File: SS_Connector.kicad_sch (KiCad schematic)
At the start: 6 parts

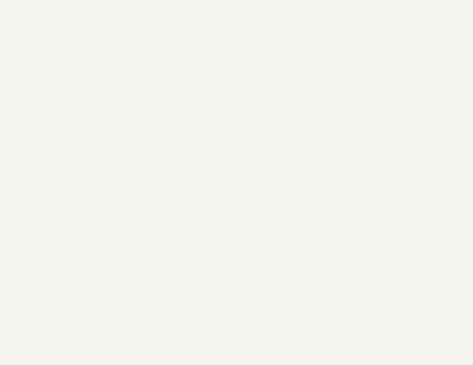
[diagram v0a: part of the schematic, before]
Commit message: MCU interfaces are done! Check the Changes and Complete ERC modifications
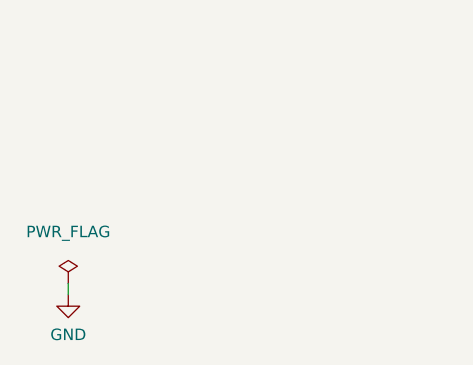
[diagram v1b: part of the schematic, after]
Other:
- company: (none) -> Parikshit Student Satellite Team
- title: (none) -> AOCS BOARD
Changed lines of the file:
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@@
 (kicad_sch (version 20211123) (generator eeschema)
   (paper "A4")
+  (title_block
+    (title "AOCS BOARD")
+    (company "Parikshit Student Satellite Team")
+  )
   (junction (at 199.39 45.72) (diameter 0) (color 0 0 0 0)
   )
@@
   )
   (wire (pts (xy 41.91 119.38) (xy 46.99 119.38))
+    (stroke (width 0) (type default) (color 0 0 0 0))
+  )
+  (wire (pts (xy 18.415 179.07) (xy 18.415 177.8))
     (stroke (width 0) (type default) (color 0 0 0 0))
   )
@@
   (symbol (lib_id "power:GND") (at 144.78 135.89 0) (unit 1)
     (in_bom yes) (on_board yes) (fields_autoplaced)
-    (property "Reference" "#PWR?" (id 0) (at 144.78 142.24 0)
+    (property "Reference" "#PWR0259" (id 0) (at 144.78 142.24 0)
       (effects (font (size 1.27 1.27)) hide)
     )
@@
   (symbol (lib_id "power:GND") (at 114.3 119.38 0) (unit 1)
     (in_bom yes) (on_board yes) (fields_autoplaced)
-    (property "Reference" "#PWR?" (id 0) (at 114.3 125.73 0)
+    (property "Reference" "#PWR0260" (id 0) (at 114.3 125.73 0)
       (effects (font (size 1.27 1.27)) hide)
     )
@@
   (symbol (lib_id "power:GND") (at 110.49 46.99 0) (unit 1)
     (in_bom yes) (on_board yes) (fields_autoplaced)
-    (property "Reference" "#PWR?" (id 0) (at 110.49 53.34 0)
+    (property "Reference" "#PWR0258" (id 0) (at 110.49 53.34 0)
       (effects (font (size 1.27 1.27)) hide)
     )
@@
   (symbol (lib_id "power:GND") (at 204.47 119.38 0) (unit 1)
     (in_bom yes) (on_board yes) (fields_autoplaced)
-    (property "Reference" "#PWR?" (id 0) (at 204.47 125.73 0)
+    (property "Reference" "#PWR0264" (id 0) (at 204.47 125.73 0)
       (effects (font (size 1.27 1.27)) hide)
     )
@@
     (pin "1")
   )
+  (symbol (lib_id "power:PWR_FLAG") (at 18.415 177.8 0) (unit 1)
+    (in_bom yes) (on_board yes) (fields_autoplaced)
+    (property "Reference" "#FLG0116" (id 0) (at 18.415 175.895 0)
+      (effects (font (size 1.27 1.27)) hide)
+    )
+    (property "Value" "PWR_FLAG" (id 1) (at 18.415 172.085 0))
+    (property "Footprint" "" (id 2) (at 18.415 177.8 0)
+      (effects (font (size 1.27 1.27)) hide)
+    )
+    (property "Datasheet" "~" (id 3) (at 18.415 177.8 0)
+      (effects (font (size 1.27 1.27)) hide)
+    )
+    (pin "1")
+  )
   (symbol (lib_id "power:GND") (at 73.66 135.89 0) (unit 1)
     (in_bom yes) (on_board yes) (fields_autoplaced)
-    (property "Reference" "#PWR?" (id 0) (at 73.66 142.24 0)
+    (property "Reference" "#PWR0253" (id 0) (at 73.66 142.24 0)
       (effects (font (size 1.27 1.27)) hide)
     )
@@
   (symbol (lib_id "power:GND") (at 199.39 48.26 0) (unit 1)
     (in_bom yes) (on_board yes) (fields_autoplaced)
-    (property "Reference" "#PWR?" (id 0) (at 199.39 54.61 0)
+    (property "Reference" "#PWR0255" (id 0) (at 199.39 54.61 0)
       (effects (font (size 1.27 1.27)) hide)
     )
@@
   (symbol (lib_id "power:GND") (at 41.91 121.92 0) (unit 1)
     (in_bom yes) (on_board yes) (fields_autoplaced)
-    (property "Reference" "#PWR?" (id 0) (at 41.91 128.27 0)
+    (property "Reference" "#PWR0254" (id 0) (at 41.91 128.27 0)
       (effects (font (size 1.27 1.27)) hide)
     )
@@
   (symbol (lib_id "power:GND") (at 142.24 63.5 0) (unit 1)
     (in_bom yes) (on_board yes) (fields_autoplaced)
-    (property "Reference" "#PWR?" (id 0) (at 142.24 69.85 0)
+    (property "Reference" "#PWR0257" (id 0) (at 142.24 69.85 0)
       (effects (font (size 1.27 1.27)) hide)
     )
@@
   (symbol (lib_id "power:GND") (at 232.41 133.35 0) (unit 1)
     (in_bom yes) (on_board yes) (fields_autoplaced)
-    (property "Reference" "#PWR?" (id 0) (at 232.41 139.7 0)
+    (property "Reference" "#PWR0263" (id 0) (at 232.41 139.7 0)
       (effects (font (size 1.27 1.27)) hide)
     )
@@
   (symbol (lib_id "power:GND") (at 50.8 48.26 0) (unit 1)
     (in_bom yes) (on_board yes) (fields_autoplaced)
-    (property "Reference" "#PWR?" (id 0) (at 50.8 54.61 0)
+    (property "Reference" "#PWR0261" (id 0) (at 50.8 54.61 0)
       (effects (font (size 1.27 1.27)) hide)
     )
@@
     (pin "MP2")
   )
+  (symbol (lib_id "power:GND") (at 18.415 179.07 0) (unit 1)
+    (in_bom yes) (on_board yes) (fields_autoplaced)
+    (property "Reference" "#PWR0280" (id 0) (at 18.415 185.42 0)
+      (effects (font (size 1.27 1.27)) hide)
+    )
+    (property "Value" "GND" (id 1) (at 18.415 183.515 0))
+    (property "Footprint" "" (id 2) (at 18.415 179.07 0)
+      (effects (font (size 1.27 1.27)) hide)
+    )
+    (property "Datasheet" "" (id 3) (at 18.415 179.07 0)
+      (effects (font (size 1.27 1.27)) hide)
+    )
+    (pin "1")
+  )
   (symbol (lib_id "power:GND") (at 229.87 63.5 0) (unit 1)
     (in_bom yes) (on_board yes) (fields_autoplaced)
-    (property "Reference" "#PWR?" (id 0) (at 229.87 69.85 0)
+    (property "Reference" "#PWR0256" (id 0) (at 229.87 69.85 0)
       (effects (font (size 1.27 1.27)) hide)
     )
@@
   (symbol (lib_id "power:GND") (at 78.74 63.5 0) (unit 1)
     (in_bom yes) (on_board yes) (fields_autoplaced)
-    (property "Reference" "#PWR?" (id 0) (at 78.74 69.85 0)
-      (effects (font (size 1.27 1.27)) hide)
-    )
+    (property "Reference" "#PWR0262" (id 0) (at 78.74 69.85 0)
+      (effects (font (size 1.27 1.27)) hide)
+    )

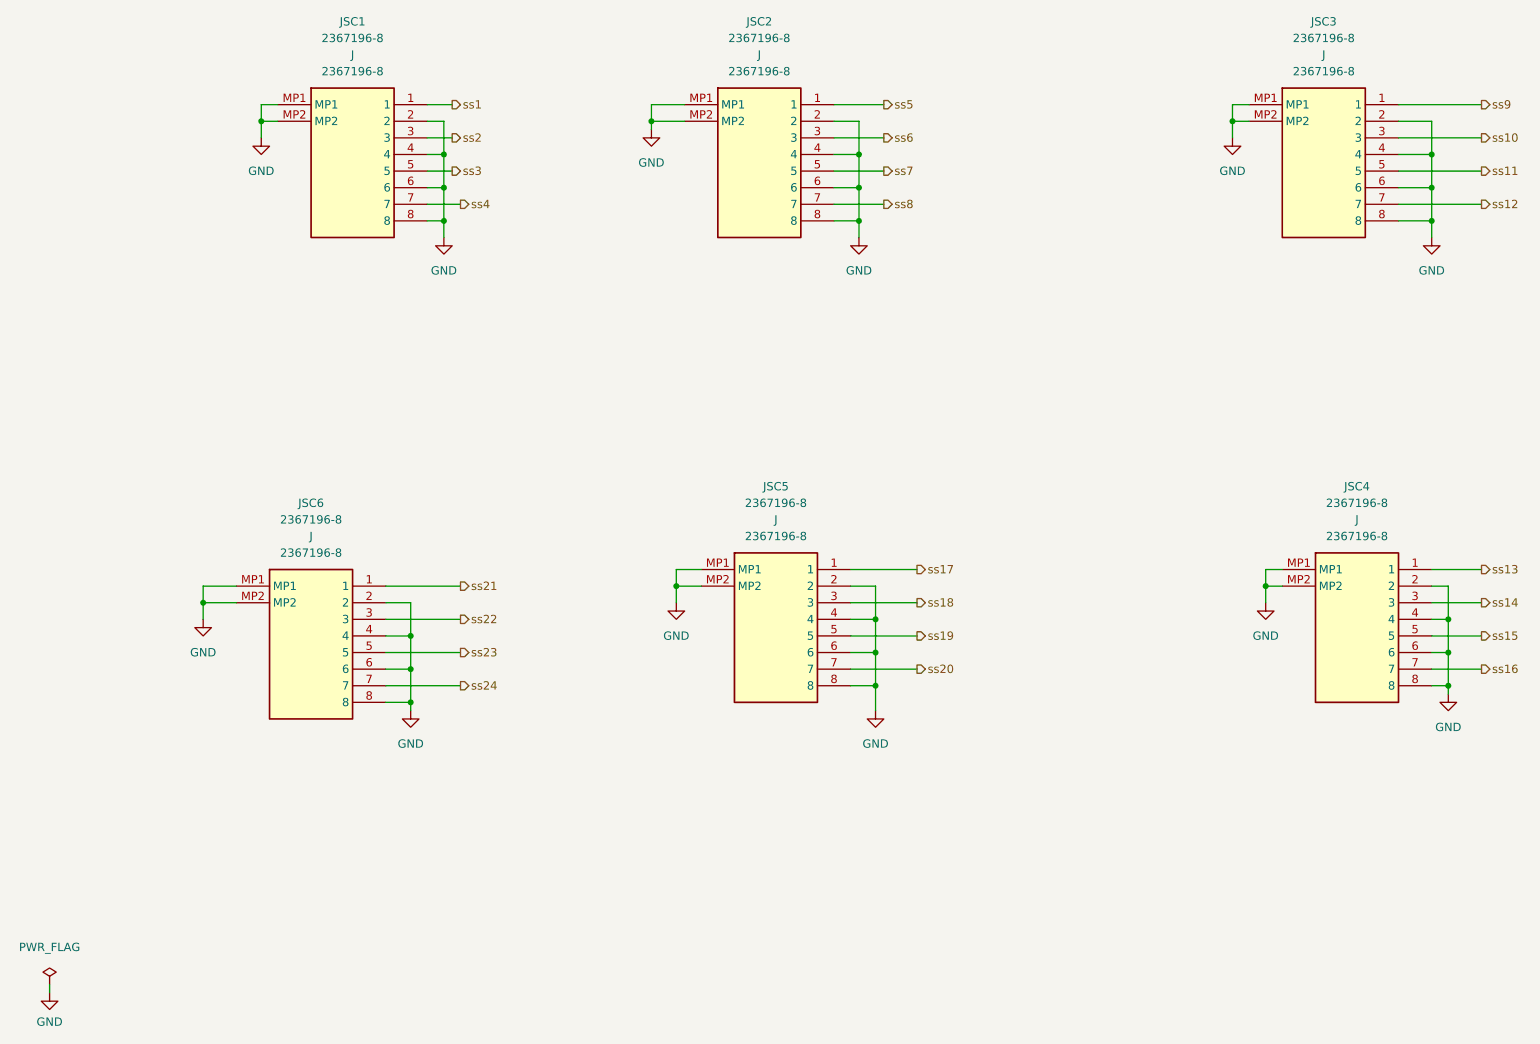
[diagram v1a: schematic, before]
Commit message: Max ERC errors corrected
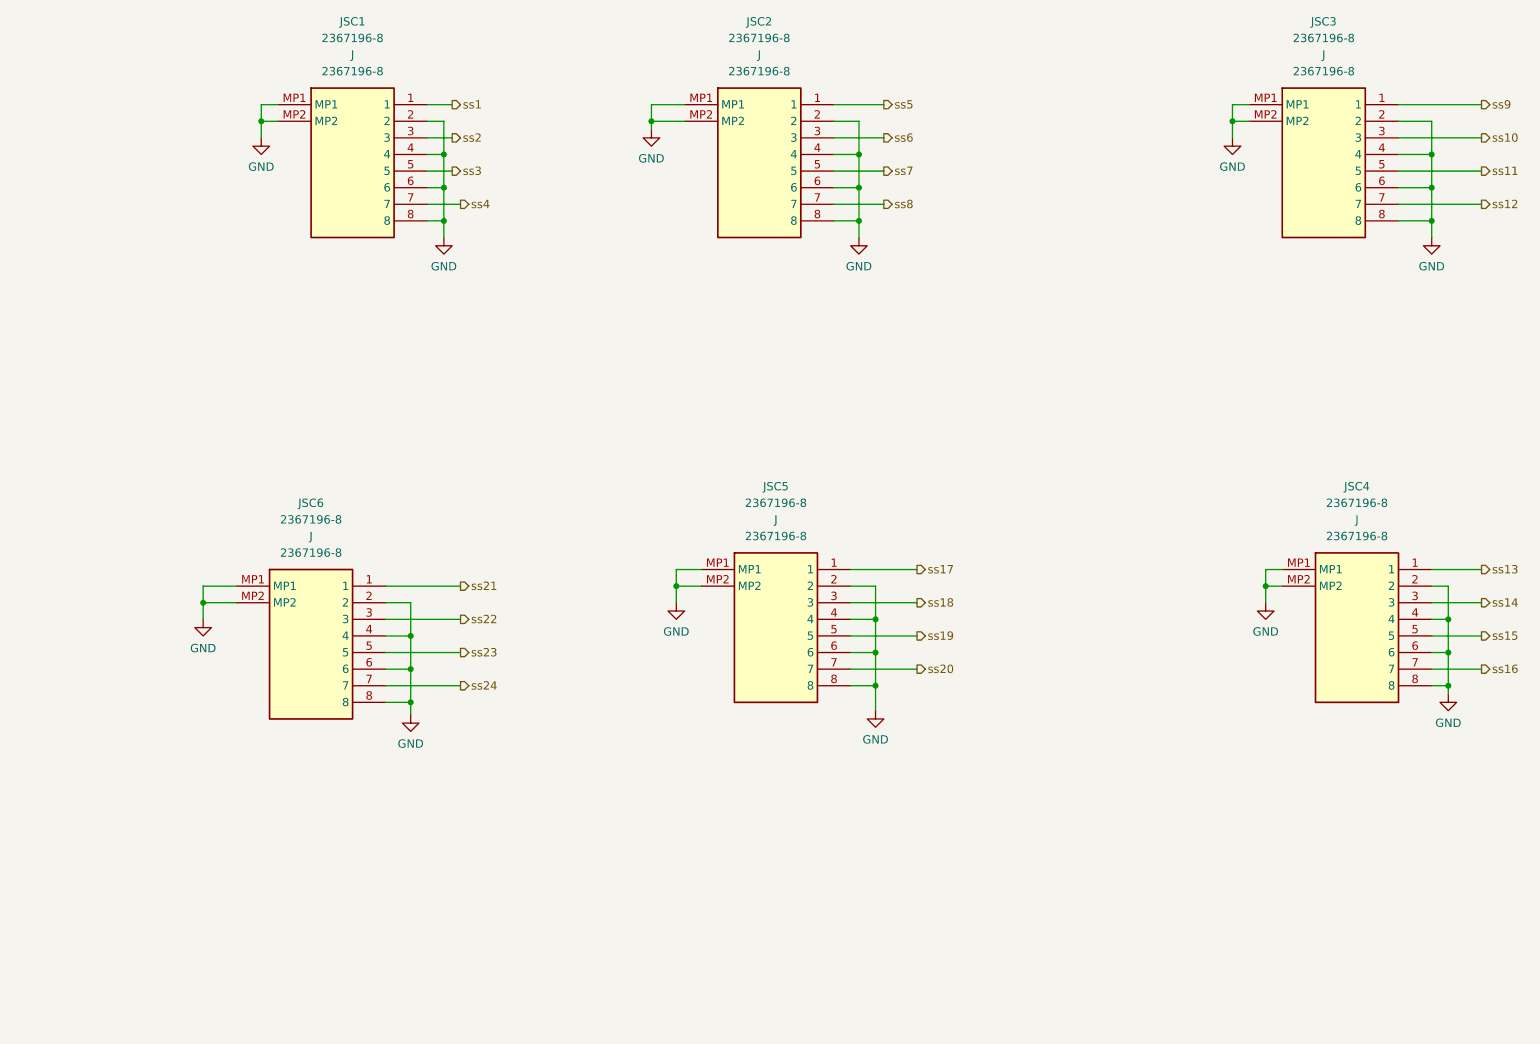
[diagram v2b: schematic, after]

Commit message: Updated the changes
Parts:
- renumbered JSC1 to JSC2, JSC2 to JSC3, JSC3 to JSC4, JSC4 to JSC6, JSC6 to JSC7
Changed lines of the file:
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@@
   (symbol (lib_id "2367196-8:2367196-8") (at 207.01 114.3 0) (unit 1)
     (in_bom yes) (on_board yes) (fields_autoplaced)
-    (property "Reference" "JSC4" (id 0) (at 218.44 101.6 0))
+    (property "Reference" "JSC6" (id 0) (at 218.44 101.6 0))
     (property "Value" "2367196-8" (id 1) (at 218.44 104.14 0))
     (property "Footprint" "" (id 2) (at 207.01 114.3 0)
@@
   (symbol (lib_id "2367196-8:2367196-8") (at 115.57 43.18 0) (unit 1)
     (in_bom yes) (on_board yes) (fields_autoplaced)
-    (property "Reference" "JSC2" (id 0) (at 127 30.48 0))
+    (property "Reference" "JSC3" (id 0) (at 127 30.48 0))
     (property "Value" "2367196-8" (id 1) (at 127 33.02 0))
     (property "Footprint" "" (id 2) (at 115.57 43.18 0)
@@
   (symbol (lib_id "upsat-comms-hardware:GND") (at 110.49 46.99 0) (unit 1)
     (in_bom yes) (on_board yes) (fields_autoplaced)
-    (property "Reference" "#PWR0258" (id 0) (at 110.49 53.34 0)
+    (property "Reference" "#PWR0155" (id 0) (at 110.49 53.34 0)
       (effects (font (size 1.27 1.27)) hide)
     )
@@
   (symbol (lib_id "upsat-comms-hardware:GND") (at 199.39 48.26 0) (unit 1)
     (in_bom yes) (on_board yes) (fields_autoplaced)
-    (property "Reference" "#PWR0255" (id 0) (at 199.39 54.61 0)
+    (property "Reference" "#PWR0157" (id 0) (at 199.39 54.61 0)
       (effects (font (size 1.27 1.27)) hide)
     )
@@
   (symbol (lib_id "upsat-comms-hardware:GND") (at 73.66 136.525 0) (unit 1)
     (in_bom yes) (on_board yes) (fields_autoplaced)
-    (property "Reference" "#PWR0253" (id 0) (at 73.66 142.875 0)
+    (property "Reference" "#PWR0166" (id 0) (at 73.66 142.875 0)
       (effects (font (size 1.27 1.27)) hide)
     )
@@
   (symbol (lib_id "upsat-comms-hardware:GND") (at 78.74 63.5 0) (unit 1)
     (in_bom yes) (on_board yes) (fields_autoplaced)
-    (property "Reference" "#PWR0262" (id 0) (at 78.74 69.85 0)
+    (property "Reference" "#PWR0158" (id 0) (at 78.74 69.85 0)
       (effects (font (size 1.27 1.27)) hide)
     )
@@
   (symbol (lib_id "upsat-comms-hardware:GND") (at 41.91 121.92 0) (unit 1)
     (in_bom yes) (on_board yes) (fields_autoplaced)
-    (property "Reference" "#PWR0254" (id 0) (at 41.91 128.27 0)
+    (property "Reference" "#PWR0163" (id 0) (at 41.91 128.27 0)
       (effects (font (size 1.27 1.27)) hide)
     )
@@
   (symbol (lib_id "upsat-comms-hardware:GND") (at 114.3 119.38 0) (unit 1)
     (in_bom yes) (on_board yes) (fields_autoplaced)
-    (property "Reference" "#PWR0259" (id 0) (at 114.3 125.73 0)
+    (property "Reference" "#PWR0161" (id 0) (at 114.3 125.73 0)
       (effects (font (size 1.27 1.27)) hide)
     )
@@
   (symbol (lib_id "2367196-8:2367196-8") (at 201.93 43.18 0) (unit 1)
     (in_bom yes) (on_board yes) (fields_autoplaced)
-    (property "Reference" "JSC3" (id 0) (at 213.36 30.48 0))
+    (property "Reference" "JSC4" (id 0) (at 213.36 30.48 0))
     (property "Value" "2367196-8" (id 1) (at 213.36 33.02 0))
     (property "Footprint" "" (id 2) (at 201.93 43.18 0)
@@
   (symbol (lib_id "2367196-8:2367196-8") (at 53.34 43.18 0) (unit 1)
     (in_bom yes) (on_board yes) (fields_autoplaced)
-    (property "Reference" "JSC1" (id 0) (at 64.77 30.48 0))
+    (property "Reference" "JSC2" (id 0) (at 64.77 30.48 0))
     (property "Value" "2367196-8" (id 1) (at 64.77 33.02 0))
     (property "Footprint" "" (id 2) (at 53.34 43.18 0)
@@
   (symbol (lib_id "upsat-comms-hardware:GND") (at 50.8 48.26 0) (unit 1)
     (in_bom yes) (on_board yes) (fields_autoplaced)
-    (property "Reference" "#PWR0261" (id 0) (at 50.8 54.61 0)
+    (property "Reference" "#PWR0156" (id 0) (at 50.8 54.61 0)
       (effects (font (size 1.27 1.27)) hide)
     )
@@
   (symbol (lib_id "upsat-comms-hardware:GND") (at 142.24 63.5 0) (unit 1)
     (in_bom yes) (on_board yes) (fields_autoplaced)
-    (property "Reference" "#PWR0257" (id 0) (at 142.24 69.85 0)
+    (property "Reference" "#PWR0159" (id 0) (at 142.24 69.85 0)
       (effects (font (size 1.27 1.27)) hide)
     )
@@
   (symbol (lib_id "upsat-comms-hardware:GND") (at 232.41 133.35 0) (unit 1)
     (in_bom yes) (on_board yes) (fields_autoplaced)
-    (property "Reference" "#PWR0264" (id 0) (at 232.41 139.7 0)
+    (property "Reference" "#PWR0164" (id 0) (at 232.41 139.7 0)
       (effects (font (size 1.27 1.27)) hide)
     )
@@
   (symbol (lib_id "upsat-comms-hardware:GND") (at 229.87 63.5 0) (unit 1)
     (in_bom yes) (on_board yes) (fields_autoplaced)
-    (property "Reference" "#PWR0256" (id 0) (at 229.87 69.85 0)
+    (property "Reference" "#PWR0160" (id 0) (at 229.87 69.85 0)
       (effects (font (size 1.27 1.27)) hide)
     )
@@
   (symbol (lib_id "2367196-8:2367196-8") (at 46.99 116.84 0) (unit 1)
     (in_bom yes) (on_board yes) (fields_autoplaced)
-    (property "Reference" "JSC6" (id 0) (at 58.42 104.14 0))
+    (property "Reference" "JSC7" (id 0) (at 58.42 104.14 0))
     (property "Value" "2367196-8" (id 1) (at 58.42 106.68 0))
     (property "Footprint" "" (id 2) (at 46.99 116.84 0)
@@
   (symbol (lib_id "upsat-comms-hardware:GND") (at 144.78 135.89 0) (unit 1)
     (in_bom yes) (on_board yes) (fields_autoplaced)
-    (property "Reference" "#PWR0260" (id 0) (at 144.78 142.24 0)
+    (property "Reference" "#PWR0165" (id 0) (at 144.78 142.24 0)
       (effects (font (size 1.27 1.27)) hide)
     )
@@
   (symbol (lib_id "upsat-comms-hardware:GND") (at 204.47 119.38 0) (unit 1)
     (in_bom yes) (on_board yes) (fields_autoplaced)
-    (property "Reference" "#PWR0263" (id 0) (at 204.47 125.73 0)
-      (effects (font (size 1.27 1.27)) hide)
-    )
+    (property "Reference" "#PWR0162" (id 0) (at 204.47 125.73 0)
+      (effects (font (size 1.27 1.27)) hide)
+    )
